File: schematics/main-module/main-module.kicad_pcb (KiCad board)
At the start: 4 copper layers, 134 x 52 mm, 101 parts, among them J1 Conn_01x02_Socket, J2 USB_C_Receptacle_USB2.0, J3 Charger, J4 Power, J5 Limit Switch, J6 Conn_01x04_Socket, Q1 IRLML0030, Q2 IRF7425PbF, Q3 BC847, Q4 BC847, Q6 IRLML0030, Q7 IRF7832PbF, Q8 IRF7832PbF, SW1 KLS7-TS3601-5.0-180, SW2 KLS7-TS3601-5.0-180, T1 Transformer_1P_SS, U1 CP2102N-Axx-xQFN28, U10 SRX882@315Mhz, U11 FAN3100, U12 FAN3100, U13 TMC2209_Module, U3 AMS1117-5.0, U4 AMS1117-3.3, U6 SRX882@433Mhz, U7 STX882@433Mhz, U8 ESP32-WROOM-32, U9 TL494

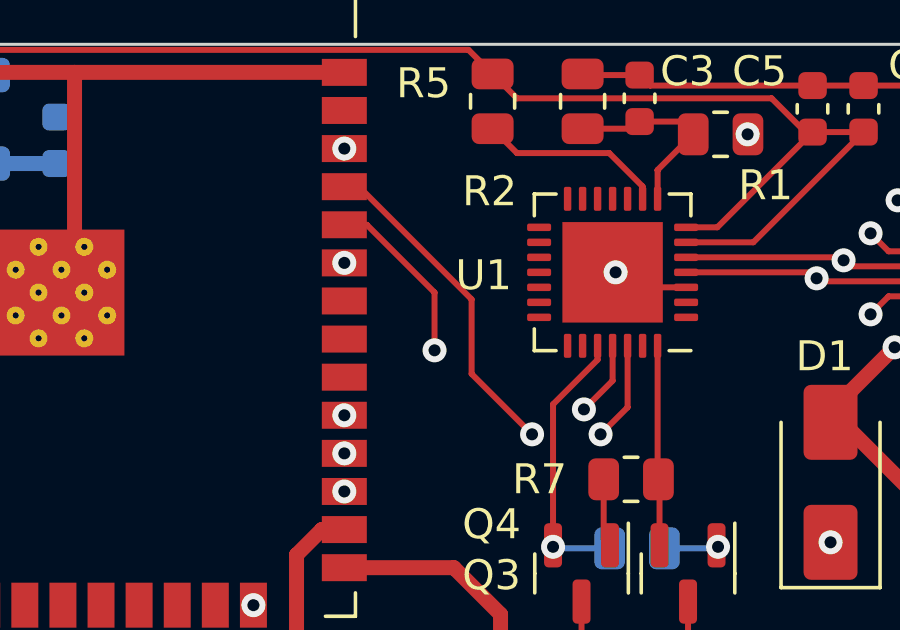
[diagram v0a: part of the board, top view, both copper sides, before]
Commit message: 1. start working under handle module; 2. rewrite stepper driver
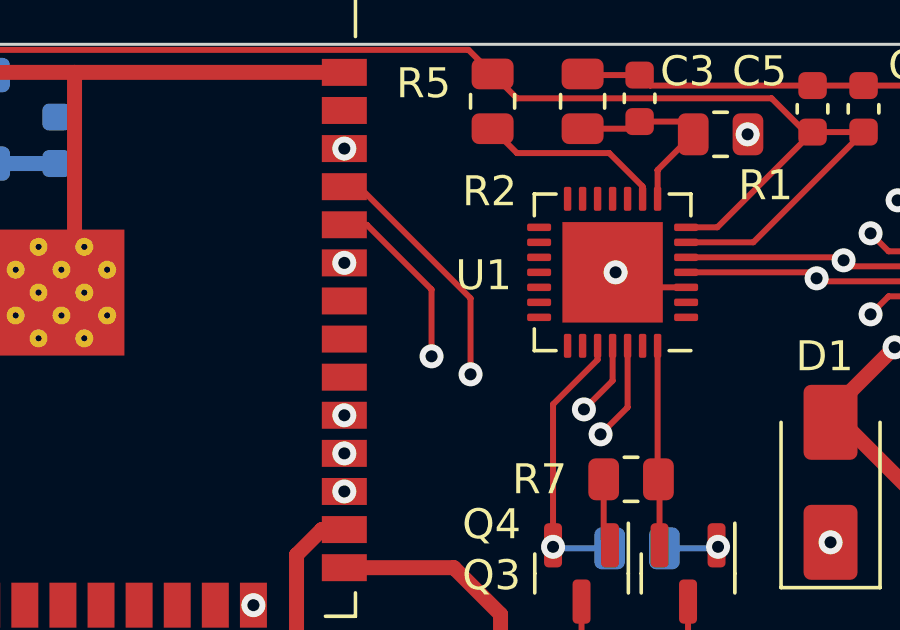
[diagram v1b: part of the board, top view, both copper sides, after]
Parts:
- C1: value 2.2 uF -> 4.7 uF
- C14, C15, C20, C24: value 100 nF -> 4.7 uF
- C16: value 1 uF -> 330 nF
- C26: value 0.1 uF -> 330 nF
- C29: value 0.1 uF -> 4.7 uF
- C31: value 100 uF -> 4.7 uF
- C34: value 100 nF -> 330 nF
- R11, R19: value 5K1 -> 22K
- R12, R20: value 10K -> 47K
- R2: value 44K -> 47K
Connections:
- U8 pad 34: /TXD_3V3 -> /RXD_3V3
- U8 pad 35: /RXD_3V3 -> /TXD_3V3

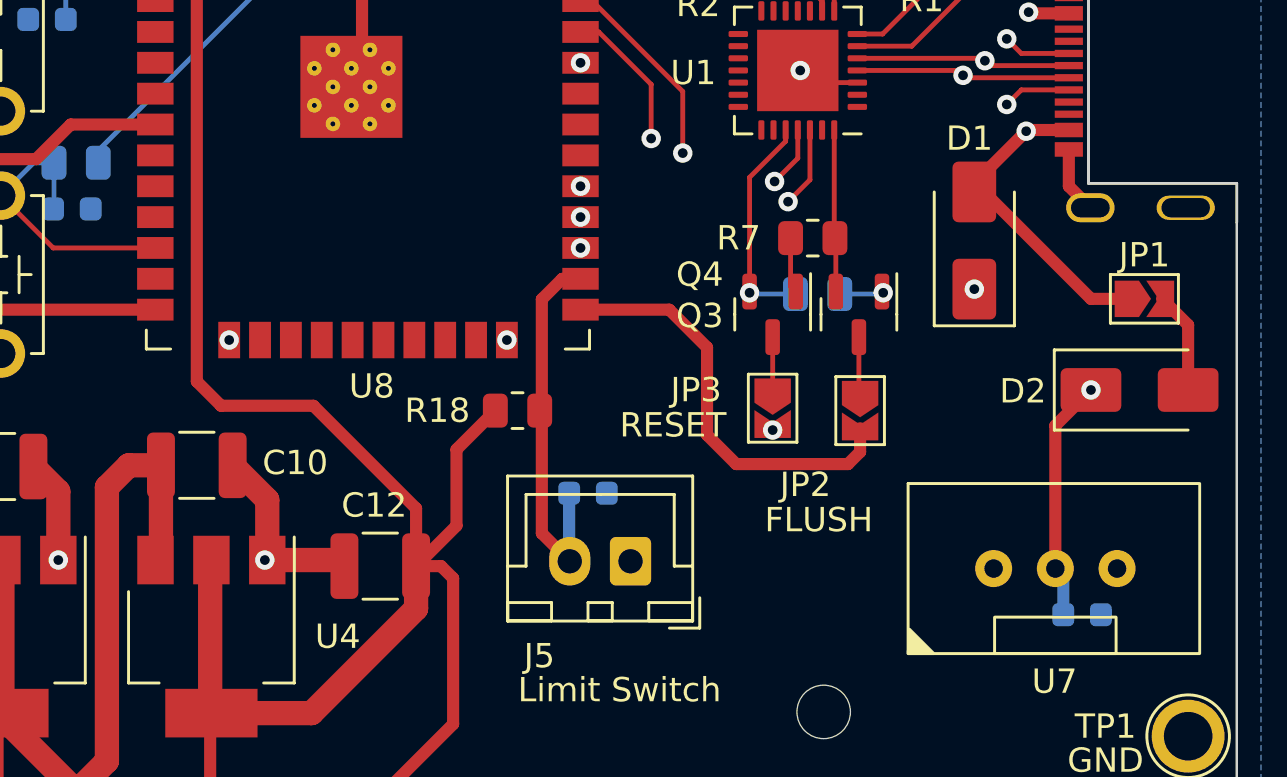
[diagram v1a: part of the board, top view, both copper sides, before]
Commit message: 1. Fixed schema - limit switch connection moved to ADC pin
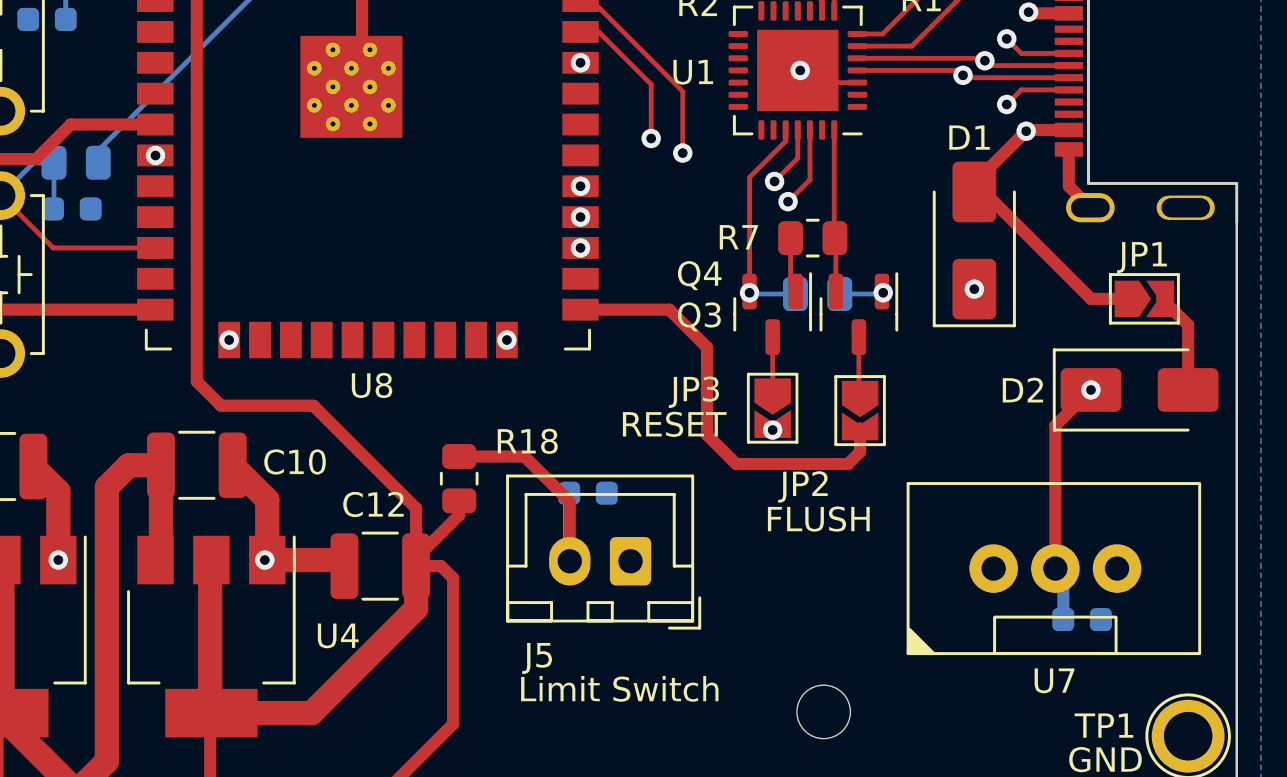
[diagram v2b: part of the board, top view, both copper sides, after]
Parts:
- moved R18 3.69 mm to (89.0, 66.4), turned to 90 degrees
- moved C14 0.20 mm to (114.6, 72.2)
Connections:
- U8 pad 26: /LIMIT_SWITCH -> unconnected-(U8-IO4-Pad26)
- U8 pad 9: unconnected-(U8-IO33-Pad9) -> /LIMIT_SWITCH
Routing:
- net /LIMIT_SWITCH: track 16.0 -> 34.5 mm, vias 0 -> 1
- net +3V3: track 213.1 -> 208.8 mm
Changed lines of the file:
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@@
   (net 77 "unconnected-(U8-IO34-Pad6)")
   (net 78 "unconnected-(U8-IO35-Pad7)")
-  (net 79 "unconnected-(U8-IO33-Pad9)")
+  (net 79 "unconnected-(U8-IO4-Pad26)")
   (net 80 "unconnected-(U8-IO26-Pad11)")
   (net 81 "unconnected-(U8-IO14-Pad13)")
@@
   )
   (footprint "Resistor_SMD:R_0805_2012Metric" (layer "F.Cu")
-    (at 91.4 63.6)
+    (at 89 66.4 90)
     (descr "Resistor SMD 0805 (2012 Metric), square (rectangular) end terminal, IPC_7351 nominal, (Body size source: IPC-SM-782 page 72, https://www.pcb-3d.com/wordpress/wp-content/uploads/ipc-sm-782a_amendment_1_and_2.pdf), generated with kicad-footprint-generator")
     (tags "resistor")
@@
     (property "ki_keywords" "R res resistor")
     (attr smd)
-    (fp_text reference "R18" (at -3.3 0) (layer "F.SilkS")
+    (fp_text reference "R18" (at 1.5 2.8 180) (layer "F.SilkS")
         (effects (font (size 1 1) (thickness 0.15)))
     )
-    (fp_text value "10K" (at 0 1.65) (layer "F.Fab")
+    (fp_text value "10K" (at 0 1.65 90) (layer "F.Fab")
         (effects (font (size 1 1) (thickness 0.15)))
     )
-    (fp_text user "${REFERENCE}" (at 0 0) (layer "F.Fab")
+    (fp_text user "${REFERENCE}" (at 0 0 90) (layer "F.Fab")
         (effects (font (size 0.5 0.5) (thickness 0.08)))
     )
@@
     (fp_line (start 1 0.625) (end -1 0.625)
       (stroke (width 0.1) (type solid)) (layer "F.Fab"))
-    (pad "1" smd roundrect (at -0.9125 0) (size 1.025 1.4) (layers "F.Cu" "F.Paste" "F.Mask") (roundrect_rratio 0.243902439)
+    (pad "1" smd roundrect (at -0.9125 0 90) (size 1.025 1.4) (layers "F.Cu" "F.Paste" "F.Mask") (roundrect_rratio 0.243902439)
       (net 4 "+3V3") (pintype "passive"))
-    (pad "2" smd roundrect (at 0.9125 0) (size 1.025 1.4) (layers "F.Cu" "F.Paste" "F.Mask") (roundrect_rratio 0.243902439)
+    (pad "2" smd roundrect (at 0.9125 0 90) (size 1.025 1.4) (layers "F.Cu" "F.Paste" "F.Mask") (roundrect_rratio 0.243902439)
       (net 28 "/LIMIT_SWITCH") (pintype "passive"))
     (model "${KICAD6_3DMODEL_DIR}/Resistor_SMD.3dshapes/R_0805_2012Metric.wrl"
@@
     (fp_rect (start -7.06 4.5) (end 6.94 -4.5)
       (stroke (width 0.05) (type default)) (fill none) (layer "F.CrtYd"))
-    (pad "2" thru_hole circle (at -2.54 0) (size 1.524 1.524) (drill 0.762) (layers "*.Cu" "*.Mask")
+    (pad "2" thru_hole circle (at -2.54 0) (size 2 2) (drill 1) (layers "*.Cu" "*.Mask")
       (net 74 "/FM_OUT_433") (pinfunction "DATA") (pintype "input"))
-    (pad "3" thru_hole circle (at 0 0) (size 1.524 1.524) (drill 0.762) (layers "*.Cu" "*.Mask")
+    (pad "3" thru_hole circle (at 0 0) (size 2 2) (drill 1) (layers "*.Cu" "*.Mask")
       (net 8 "+5V") (pinfunction "VCC") (pintype "power_in"))
-    (pad "4" thru_hole circle (at 2.54 0) (size 1.524 1.524) (drill 0.762) (layers "*.Cu" "*.Mask")
+    (pad "4" thru_hole circle (at 2.54 0) (size 2 2) (drill 1) (layers "*.Cu" "*.Mask")
       (net 2 "GNDA") (pinfunction "GND") (pintype "power_in"))
   )
@@
       (net 41 "/CHARGER_ENABLE") (pinfunction "IO32") (pintype "bidirectional"))
     (pad "9" smd rect (at -8.75 1.91) (size 1.5 0.9) (layers "F.Cu" "F.Paste" "F.Mask")
-      (net 79 "unconnected-(U8-IO33-Pad9)") (pinfunction "IO33") (pintype "bidirectional+no_connect"))
+      (net 28 "/LIMIT_SWITCH") (pinfunction "IO33") (pintype "bidirectional"))
     (pad "10" smd rect (at -8.75 3.18) (size 1.5 0.9) (layers "F.Cu" "F.Paste" "F.Mask")
       (net 101 "unconnected-(U8-IO25-Pad10)") (pinfunction "IO25") (pintype "bidirectional+no_connect"))
@@
       (net 33 "/ESP32_FLUSH") (pinfunction "IO0") (pintype "bidirectional"))
     (pad "26" smd rect (at 8.75 6.99) (size 1.5 0.9) (layers "F.Cu" "F.Paste" "F.Mask")
-      (net 28 "/LIMIT_SWITCH") (pinfunction "IO4") (pintype "bidirectional"))
+      (net 79 "unconnected-(U8-IO4-Pad26)") (pinfunction "IO4") (pintype "bidirectional+no_connect"))
     (pad "27" smd rect (at 8.75 5.72) (size 1.5 0.9) (layers "F.Cu" "F.Paste" "F.Mask")
       (net 91 "/M_DIR") (pinfunction "IO16") (pintype "bidirectional"))
@@
   )
   (footprint "Capacitor_SMD:C_0603_1608Metric" (layer "B.Cu")
-    (at 114.635 72)
+    (at 114.635 72.2)
     (descr "Capacitor SMD 0603 (1608 Metric), square (rectangular) end terminal, IPC_7351 nominal, (Body size source: IPC-SM-782 page 76, https://www.pcb-3d.com/wordpress/wp-content/uploads/ipc-sm-782a_amendment_1_and_2.pdf), generated with kicad-footprint-generator")
     (tags "capacitor")
@@
   (segment (start 101.935 44.8125) (end 103.5975 44.8125) (width 0.2) (layer "F.Cu") (net 3))
   (segment (start 111.3 44.925) (end 109.6 44.925) (width 0.2) (layer "F.Cu") (net 4))
+  (segment (start 87.225 70) (end 87.225 69.675) (width 0.5) (layer "F.Cu") (net 4))
   (segment (start 73.04 44.205) (end 76.4925 44.205) (width 0.5) (layer "F.Cu") (net 4))
   (segment (start 108.235 43.8) (end 109.36 44.925) (width 0.2) (layer "F.Cu") (net 4))
@@
   (segment (start 99.7475 43.8) (end 108.235 43.8) (width 0.2) (layer "F.Cu") (net 4))
   (segment (start 64.235 44.7) (end 65.61 43.325) (width 0.5) (layer "F.Cu") (net 4))
-  (segment (start 90.4875 63.6) (end 88.8875 65.2) (width 0.5) (layer "F.Cu") (net 4))
   (segment (start 82.925 76.05) (end 87.225 71.75) (width 1) (layer "F.Cu") (net 4))
   (segment (start 98.1325 42.185) (end 66.75 42.185) (width 0.2) (layer "F.Cu") (net 4))
@@
   (segment (start 65.61 43.325) (end 72.16 43.325) (width 0.5) (layer "F.Cu") (net 4))
   (segment (start 76.4925 44.205) (end 78.2 44.205) (width 0.5) (layer "F.Cu") (net 4))
+  (segment (start 87.225 69.675) (end 89 67.9) (width 0.5) (layer "F.Cu") (net 4))
   (segment (start 105.385 48.1) (end 106.425 48.1) (width 0.2) (layer "F.Cu") (net 4))
   (segment (start 98.935 42.9875) (end 98.1325 42.185) (width 0.2) (layer "F.Cu") (net 4))
   (segment (start 78.8 76.05) (end 82.925 76.05) (width 1) (layer "F.Cu") (net 4))
   (segment (start 78.75 76.25) (end 78.75 69.8) (width 1) (layer "F.Cu") (net 4))
+  (segment (start 89 67.9) (end 89 67.3125) (width 0.5) (layer "F.Cu") (net 4))
   (segment (start 79.2 63.4) (end 83 63.4) (width 0.5) (layer "F.Cu") (net 4))
-  (segment (start 88.8875 68.3375) (end 87.225 70) (width 0.5) (layer "F.Cu") (net 4))
   (segment (start 98.935 42.9875) (end 99.7475 43.8) (width 0.2) (layer "F.Cu") (net 4))
   (segment (start 78.2 62.4) (end 79.2 63.4) (width 0.5) (layer "F.Cu") (net 4))
@@
   (segment (start 87.225 67.625) (end 87.225 70) (width 0.5) (layer "F.Cu") (net 4))
   (segment (start 78.75 82.25) (end 78.75 76.1) (width 0.5) (layer "F.Cu") (net 4))
-  (segment (start 88.8875 65.2) (end 88.8875 68.3375) (width 0.5) (layer "F.Cu") (net 4))
   (via (at 81.6 46) (size 0.8) (drill 0.4) (layers "F.Cu" "B.Cu") (net 4))
   (via (at 59.875 85.575) (size 0.8) (drill 0.4) (layers "F.Cu" "B.Cu") (net 4))
@@
   (segment (start 96.3 83.5) (end 98.87 83.5) (width 0.5) (layer "B.Cu") (net 8))
   (segment (start 93.695 90.9) (end 96.235 90.9) (width 0.5) (layer "B.Cu") (net 8))
+  (segment (start 113.86 72.2) (end 113.86 70.425) (width 0.5) (layer "B.Cu") (net 8))
   (segment (start 98.725 91) (end 96.335 91) (width 0.5) (layer "B.Cu") (net 8))
-  (segment (start 113.86 72) (end 113.86 70.425) (width 0.5) (layer "B.Cu") (net 8))
   (segment (start 53.02 61.1) (end 59.36 61.1) (width 1) (layer "F.Cu") (net 9))
   (segment (start 59.36 61.1) (end 60.11 60.35) (width 1) (layer "F.Cu") (net 9))
@@
   (segment (start 111.435 51) (end 110.635 50.2) (width 0.2) (layer "In1.Cu") (net 24))
   (segment (start 110.635 50.2) (end 110.635 49.2) (width 0.2) (layer "In1.Cu") (net 24))
-  (segment (start 93.2425 58.175) (end 92.4 59.0175) (width 0.5) (layer "F.Cu") (net 28))
-  (segment (start 93.9925 58.175) (end 93.2425 58.175) (width 0.5) (layer "F.Cu") (net 28))
-  (segment (start 92.4 59.0175) (end 92.4 68.65) (width 0.5) (layer "F.Cu") (net 28))
-  (segment (start 92.4 68.65) (end 93.55 69.8) (width 0.5) (layer "F.Cu") (net 28))
+  (segment (start 89 65.4875) (end 91.6875 65.4875) (width 0.5) (layer "F.Cu") (net 28))
+  (segment (start 93.55 67.35) (end 93.55 69.8) (width 0.5) (layer "F.Cu") (net 28))
+  (segment (start 91.6875 65.4875) (end 93.55 67.35) (width 0.5) (layer "F.Cu") (net 28))
+  (via (at 76.5 53.1) (size 0.8) (drill 0.4) (layers "F.Cu" "B.Cu") (net 28))
+  (segment (start 93.2 69.8) (end 76.5 53.1) (width 0.5) (layer "In2.Cu") (net 28))
+  (segment (start 93.55 69.8) (end 93.2 69.8) (width 0.5) (layer "In2.Cu") (net 28))
   (segment (start 93.525 67) (end 93.525 69.775) (width 0.5) (layer "B.Cu") (net 28))
   (segment (start 49.64 78.975) (end 49.64 76.96) (width 1) (layer "F.Cu") (net 29))
